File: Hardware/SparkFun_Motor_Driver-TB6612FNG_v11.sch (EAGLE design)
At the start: 14 parts, among them U1 TB6612FNG

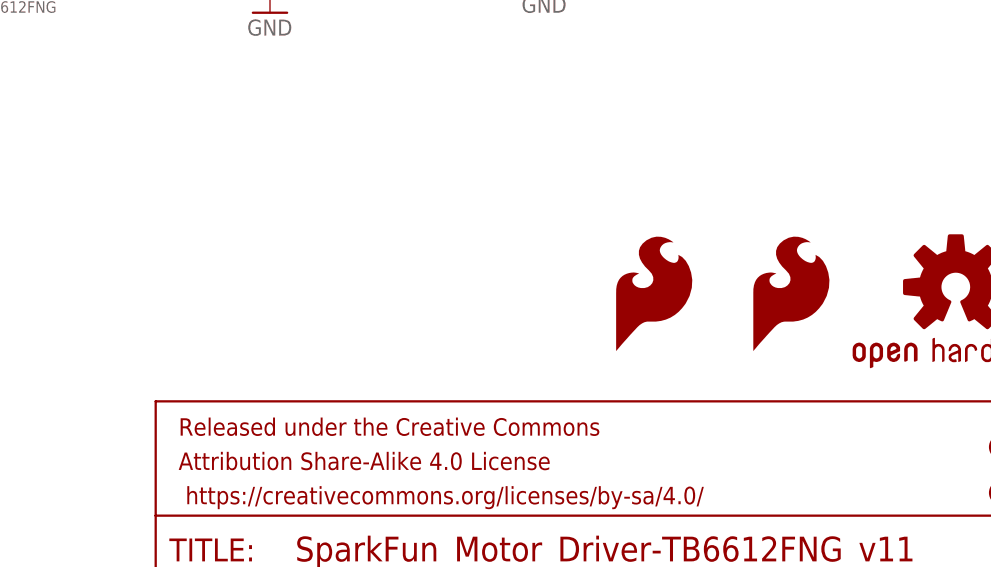
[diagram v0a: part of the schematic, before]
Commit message: Changes to design and added 1X08 conn lbr
-moved and added/removed silk
-moved fiducials and re routed some traces
-added new 1X08 offset connector lbr to repo
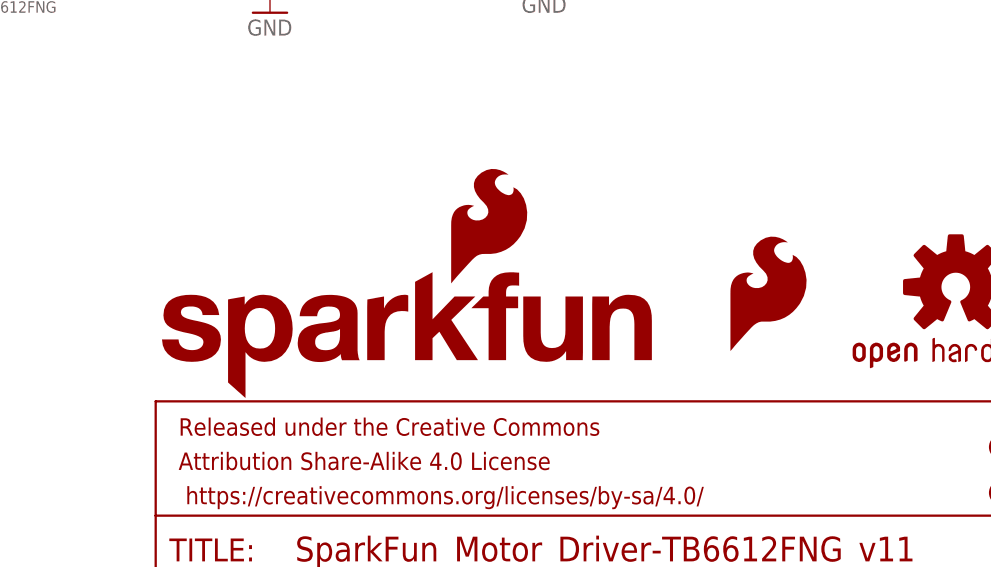
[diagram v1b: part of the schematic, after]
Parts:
- removed LOGO3: SFE_LOGO_FLAME.1_INCH, SparkFun-Aesthetics:SFE_LOGO_FLAME.1_INCH
- added LOGO4: SFE_LOGO_NAME_FLAME.1_INCH, SparkFun-Aesthetics:SFE_LOGO_NAME_FLAME.1_INCH
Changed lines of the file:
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@@
 <part name="JP8" library="SparkFun" deviceset="FIDUCIAL" device="1X2"/>
 <part name="FRAME1" library="SparkFun-Aesthetics" deviceset="FRAME-LETTER" device=""/>
-<part name="LOGO3" library="SparkFun-Aesthetics" deviceset="SFE_LOGO_FLAME" device=".1_INCH"/>
 <part name="LOGO1" library="SparkFun-Aesthetics" deviceset="SFE_LOGO_FLAME" device=".1_INCH"/>
 <part name="LOGO2" library="SparkFun-Aesthetics" deviceset="OSHW-LOGO" device="S"/>
+<part name="LOGO4" library="SparkFun-Aesthetics" deviceset="SFE_LOGO_NAME_FLAME" device=".1_INCH"/>
 </parts>
 <sheets>
@@
 <instance part="FRAME1" gate="G$1" x="0" y="0"/>
 <instance part="FRAME1" gate="V" x="147.32" y="0"/>
-<instance part="LOGO3" gate="G$1" x="198.12" y="40.64"/>
-<instance part="LOGO1" gate="G$1" x="213.36" y="40.64"/>
+<instance part="LOGO1" gate="G$1" x="210.82" y="40.64"/>
 <instance part="LOGO2" gate="G$1" x="236.22" y="48.26"/>
+<instance part="LOGO4" gate="G$1" x="147.32" y="35.56"/>
 </instances>
 <busses>

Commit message: Straightened some silk labels
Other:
- note added: "Peter Dokter"
- moved on the sheet: C1, C2, C3, JP1, JP2, U1

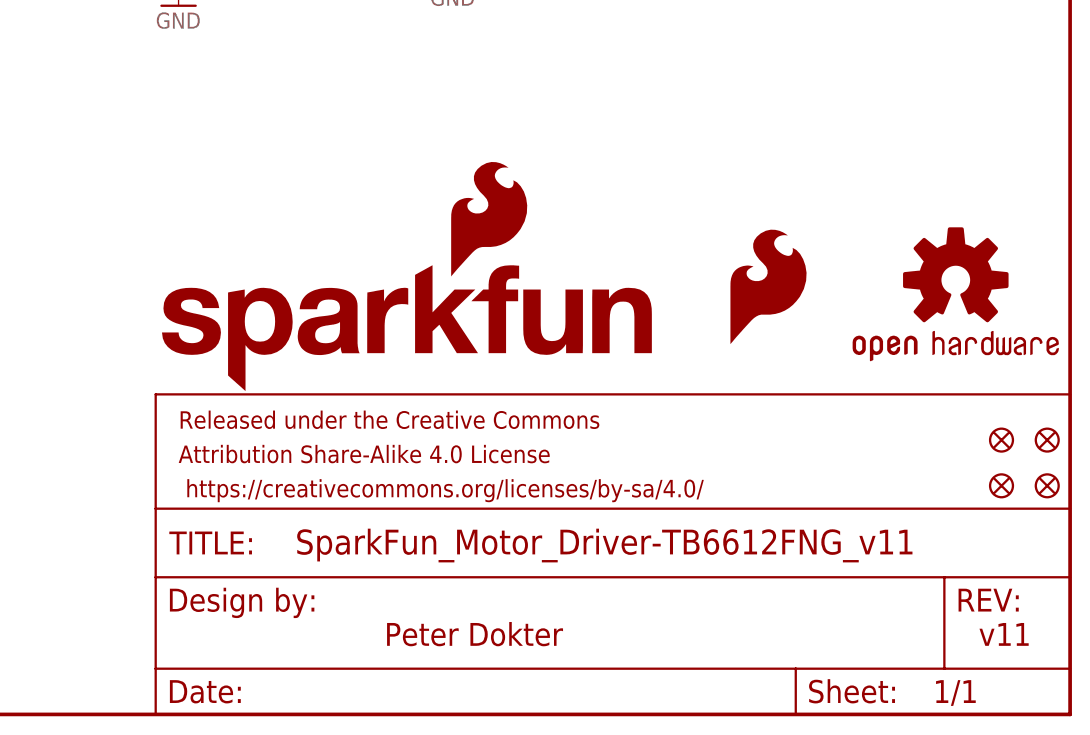
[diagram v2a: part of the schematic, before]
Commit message: Changes to SCH and BRD
-swapped to use micro-fiducials
-added revised by
-completed DRC
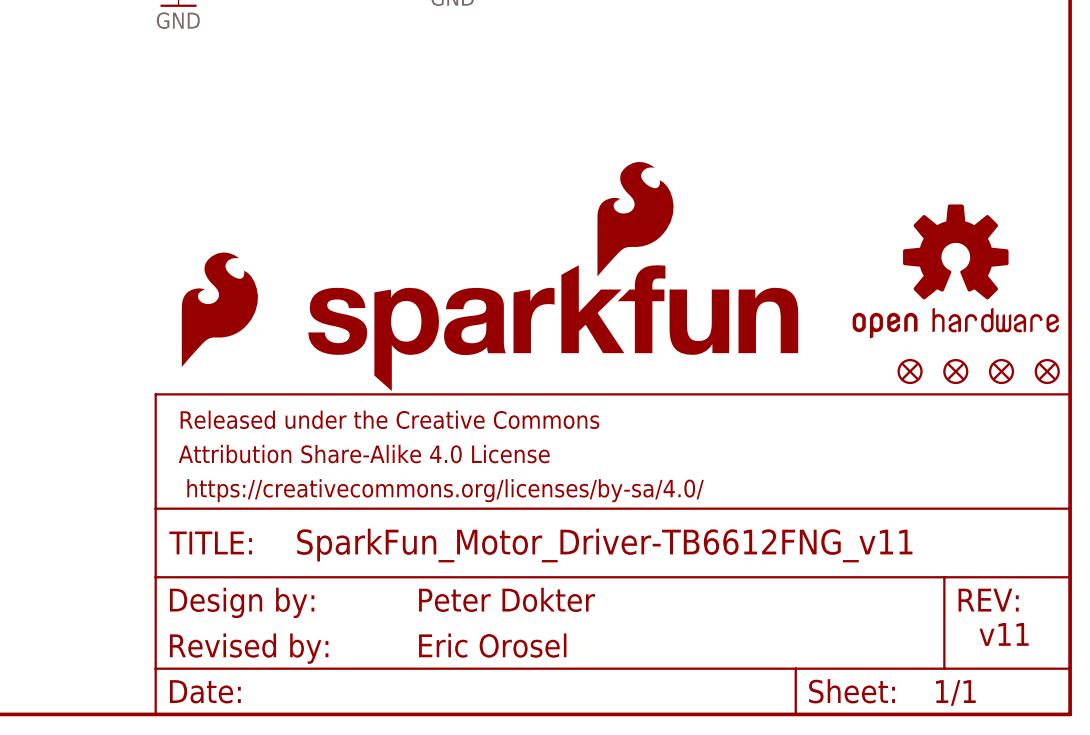
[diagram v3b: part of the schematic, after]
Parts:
- removed JP5, JP6, JP7, JP8: FIDUCIAL1X2, SparkFun:FIDUCIAL1X2
- added FD1, FD2, FD3, FD4: FIDUCIALUFIDUCIAL, SparkFun-Aesthetics:FIDUCIALUFIDUCIAL
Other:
- note added: "Eric Orosel"
- note added: "Revised by:"
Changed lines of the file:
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@@
 <part name="GND6" library="SparkFun" deviceset="GND" device=""/>
 <part name="GND7" library="SparkFun" deviceset="GND" device=""/>
-<part name="JP5" library="SparkFun" deviceset="FIDUCIAL" device="1X2"/>
-<part name="JP6" library="SparkFun" deviceset="FIDUCIAL" device="1X2"/>
-<part name="JP7" library="SparkFun" deviceset="FIDUCIAL" device="1X2"/>
-<part name="JP8" library="SparkFun" deviceset="FIDUCIAL" device="1X2"/>
 <part name="FRAME1" library="SparkFun-Aesthetics" deviceset="FRAME-LETTER" device=""/>
 <part name="LOGO1" library="SparkFun-Aesthetics" deviceset="SFE_LOGO_FLAME" device=".1_INCH"/>
 <part name="LOGO2" library="SparkFun-Aesthetics" deviceset="OSHW-LOGO" device="S"/>
 <part name="LOGO4" library="SparkFun-Aesthetics" deviceset="SFE_LOGO_NAME_FLAME" device=".1_INCH"/>
+<part name="FD1" library="SparkFun-Aesthetics" deviceset="FIDUCIAL" device="UFIDUCIAL"/>
+<part name="FD2" library="SparkFun-Aesthetics" deviceset="FIDUCIAL" device="UFIDUCIAL"/>
+<part name="FD3" library="SparkFun-Aesthetics" deviceset="FIDUCIAL" device="UFIDUCIAL"/>
+<part name="FD4" library="SparkFun-Aesthetics" deviceset="FIDUCIAL" device="UFIDUCIAL"/>
 </parts>
 <sheets>
@@
 <plain>
 <text x="238.76" y="7.62" size="2.54" layer="94">v11</text>
-<text x="172.72" y="7.62" size="2.54" layer="94">Peter Dokter</text>
+<text x="176.276" y="11.43" size="2.54" layer="94">Peter Dokter</text>
+<text x="148.59" y="6.35" size="2.54" layer="94">Revised by:</text>
+<text x="176.276" y="6.35" size="2.54" layer="94">Eric Orosel</text>
 </plain>
 <instances>
@@
 <instance part="GND6" gate="1" x="66.04" y="81.28"/>
 <instance part="GND7" gate="1" x="180.34" y="81.28"/>
-<instance part="JP5" gate="G$1" x="246.38" y="25.4"/>
-<instance part="JP6" gate="G$1" x="241.3" y="25.4"/>
-<instance part="JP7" gate="G$1" x="246.38" y="30.48"/>
-<instance part="JP8" gate="G$1" x="241.3" y="30.48"/>
 <instance part="FRAME1" gate="G$1" x="0" y="0"/>
 <instance part="FRAME1" gate="V" x="147.32" y="0"/>
-<instance part="LOGO1" gate="G$1" x="210.82" y="40.64"/>
-<instance part="LOGO2" gate="G$1" x="236.22" y="48.26"/>
-<instance part="LOGO4" gate="G$1" x="147.32" y="35.56"/>
+<instance part="LOGO1" gate="G$1" x="149.86" y="38.1"/>
+<instance part="LOGO2" gate="G$1" x="236.22" y="50.8"/>
+<instance part="LOGO4" gate="G$1" x="163.576" y="35.56"/>
+<instance part="FD1" gate="G$1" x="246.38" y="38.1" rot="R90"/>
+<instance part="FD2" gate="G$1" x="241.3" y="38.1" rot="R90"/>
+<instance part="FD3" gate="G$1" x="236.22" y="38.1" rot="R90"/>
+<instance part="FD4" gate="G$1" x="231.14" y="38.1" rot="R90"/>
 </instances>
 <busses>

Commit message: changed header
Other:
- moved on the sheet: JP1, JP2

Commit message: updated part lbr
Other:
- moved on the sheet: JP1, JP2
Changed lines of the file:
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@@
 <layer number="230" name="230bmp" color="12" fill="1" visible="yes" active="yes"/>
 <layer number="231" name="231bmp" color="9" fill="1" visible="yes" active="yes"/>
+<layer number="232" name="Eagle3D_PG2" color="7" fill="1" visible="yes" active="yes"/>
+<layer number="233" name="Eagle3D_PG3" color="7" fill="1" visible="yes" active="yes"/>
 <layer number="248" name="Housing" color="7" fill="1" visible="yes" active="yes"/>
 <layer number="249" name="Edge" color="7" fill="1" visible="yes" active="yes"/>

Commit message: Changed cap parts and added measures
-Replaced 0603 caps with caps from the sparkfun-capacitors lbr
-Replaced 10uf cap with cap from the sparkfun-capacitors lbr
-added measures to the design
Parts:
- C1, C2: device SparkFun:CAP0402-CAP -> SparkFun-Capacitors:0.1UF-0402-16V-10%
- C3: value 10uf , 20V -> 10uF; device SparkFun:CAP_POL3528 -> SparkFun-Capacitors:10UF-POLAR-EIA3528-20V-10%(TANT)
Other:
- note added: "VMAX=15V VCC=2.7-5.5V"
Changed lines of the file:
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@@
 <parts>
 <part name="U1" library="SparkFun-IC-Special-Function" deviceset="TB6612FNG" device="" value="TB6612FNG"/>
-<part name="C1" library="SparkFun" deviceset="CAP" device="0402-CAP" value="0.1uF"/>
-<part name="C2" library="SparkFun" deviceset="CAP" device="0402-CAP" value="0.1uF"/>
-<part name="C3" library="SparkFun" deviceset="CAP_POL" device="3528" value="10uf , 20V"/>
+<part name="C1" library="SparkFun-Capacitors" deviceset="0.1UF" device="-0402-16V-10%" value="0.1uF"/>
+<part name="C2" library="SparkFun-Capacitors" deviceset="0.1UF" device="-0402-16V-10%" value="0.1uF"/>
+<part name="C3" library="SparkFun-Capacitors" deviceset="10UF-POLAR" device="-EIA3528-20V-10%(TANT)" value="10uF"/>
 <part name="JP1" library="Testing" deviceset="M08" device="75_PERCENT_REDUCED"/>
 <part name="JP2" library="Testing" deviceset="M08" device="75_PERCENT_REDUCED"/>
@@
 <text x="148.59" y="6.35" size="2.54" layer="94">Revised by:</text>
 <text x="176.276" y="6.35" size="2.54" layer="94">Eric Orosel</text>
+<text x="109.22" y="60.96" size="2.54" layer="94">VMAX=15V
+VCC=2.7-5.5V</text>
 </plain>
 <instances>
@@
 </schematic>
 </drawing>
+<compatibility>
+<note version="6.3" minversion="6.2.2" severity="warning">
+Since Version 6.2.2 text objects can contain more than one line,
+which will not be processed correctly with this version.
+</note>
+</compatibility>
 </eagle>
